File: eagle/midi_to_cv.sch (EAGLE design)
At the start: 45 parts, among them IC2 4504N, IC3 4099N, U1 ATMEGA328P_PDIP

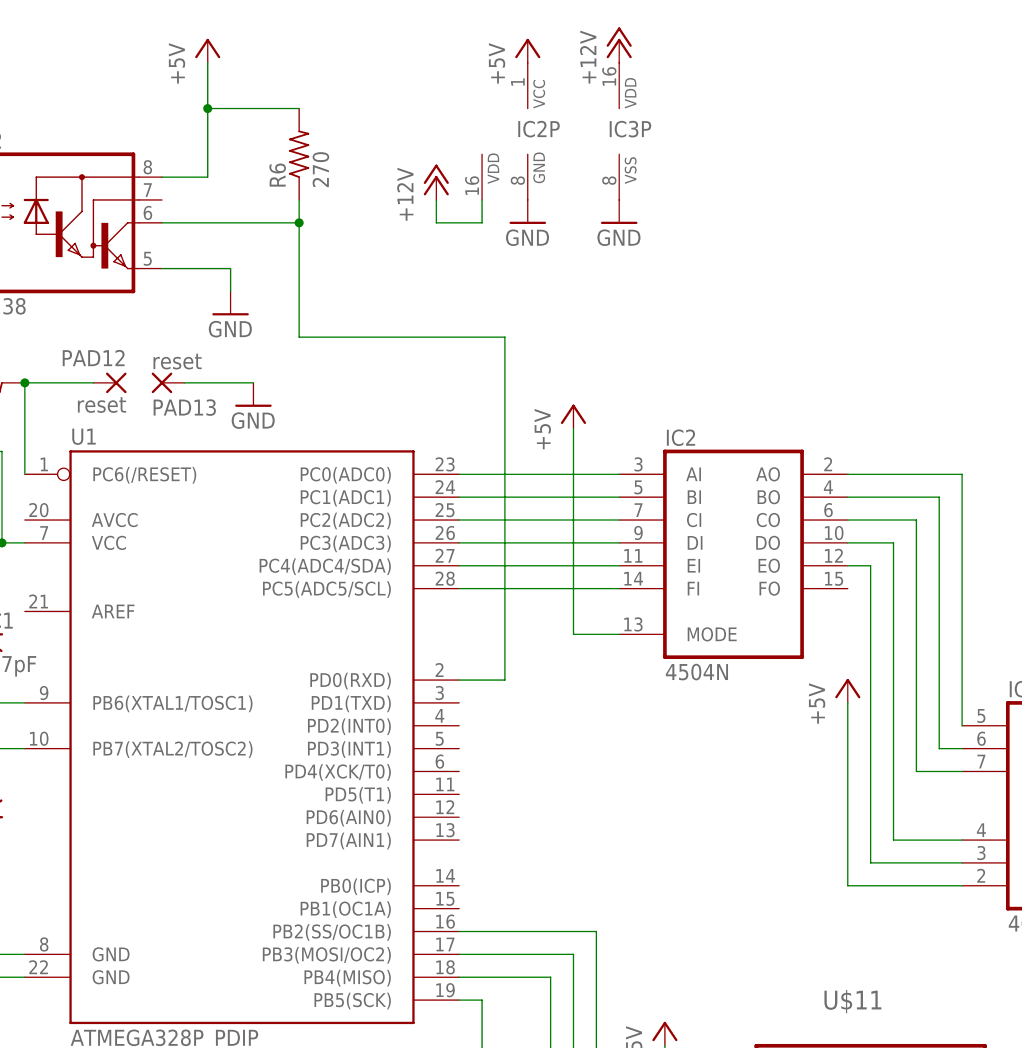
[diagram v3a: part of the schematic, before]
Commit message: connected midi to serial in
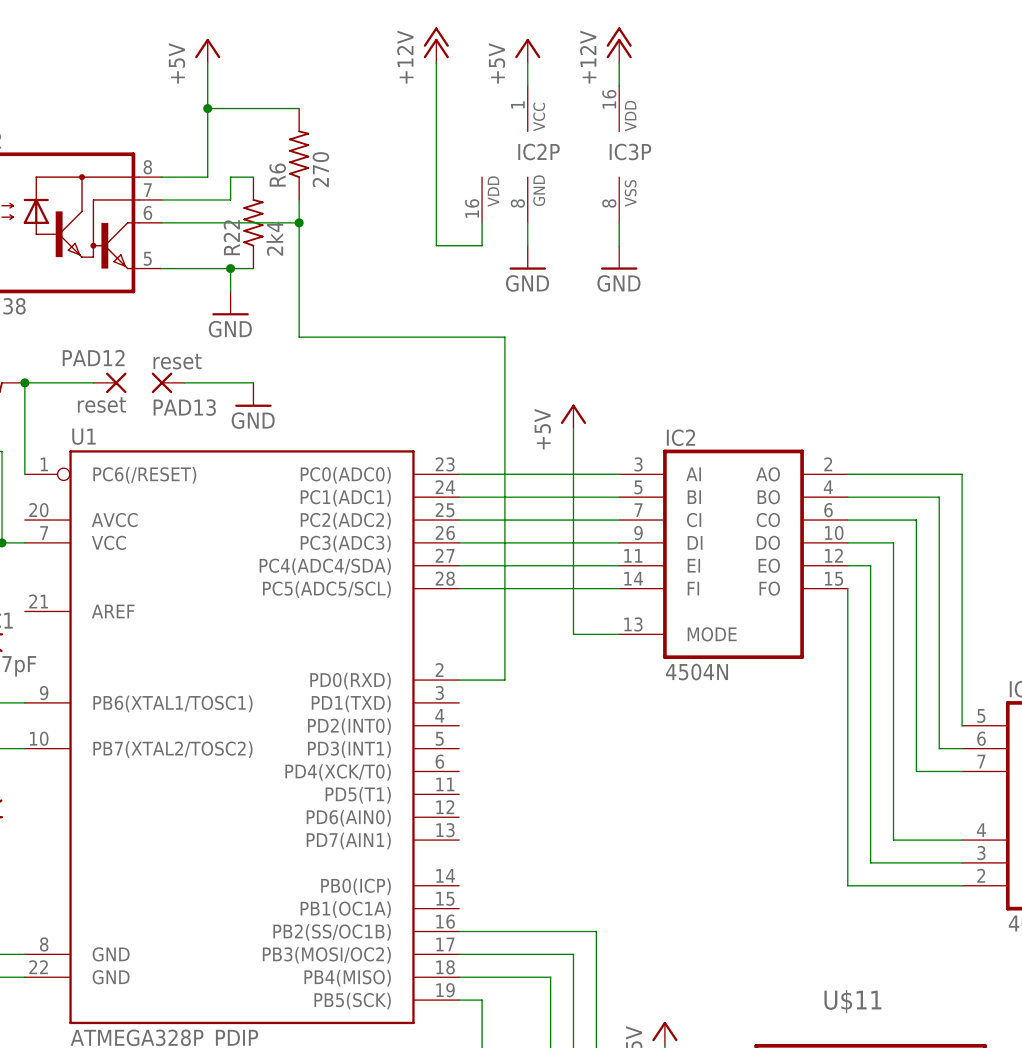
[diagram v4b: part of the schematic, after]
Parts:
- added R22: 2k4, rcl:R-US_0207/10
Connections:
- removed net N$30: U1.PD0(RXD)
- new net N$60: OK2.VB, R22.2
- new net N$61: IC2A.FO, IC3A.CLR
- net +5V: no longer IC3A.CLR
- net GND: now also R22.1
- net N$20: now also U1.PD0(RXD)
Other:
- moved on the sheet: IC2P, IC3P
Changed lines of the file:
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@@
 <part name="MIDI_IN" library="con-molex" deviceset="22-23-2021" device=""/>
 <part name="GND4" library="supply1" deviceset="GND" device=""/>
-<part name="P+2" library="supply1" deviceset="+5V" device=""/>
 <part name="U$11" library="Texas Instruments_By_element14_Batch_1" deviceset="TLV5628C/I" device=""/>
 <part name="P+5" library="supply1" deviceset="+5V" device=""/>
@@
 <part name="JP2" library="pinhead" deviceset="PINHD-1X8" device=""/>
 <part name="JP3" library="pinhead" deviceset="PINHD-1X8" device=""/>
+<part name="R22" library="rcl" deviceset="R-US_" device="0207/10" value="2k4"/>
 </parts>
 <sheets>
@@
 <instance part="R15" gate="G$1" x="-20.32" y="45.72" rot="R90"/>
 <instance part="IC2" gate="A" x="73.66" y="66.04"/>
-<instance part="IC2" gate="P" x="50.8" y="111.76"/>
+<instance part="IC2" gate="P" x="50.8" y="109.22"/>
 <instance part="IC3" gate="A" x="111.76" y="38.1"/>
-<instance part="IC3" gate="P" x="60.96" y="111.76"/>
+<instance part="IC3" gate="P" x="60.96" y="109.22"/>
 <instance part="P+4" gate="1" x="50.8" y="121.92"/>
-<instance part="P+8" gate="1" x="40.64" y="106.68"/>
-<instance part="GND3" gate="1" x="50.8" y="101.6"/>
-<instance part="GND16" gate="1" x="60.96" y="101.6"/>
+<instance part="P+8" gate="1" x="40.64" y="121.92"/>
+<instance part="GND3" gate="1" x="50.8" y="96.52"/>
+<instance part="GND16" gate="1" x="60.96" y="96.52"/>
 <instance part="P+15" gate="1" x="60.96" y="121.92"/>
 <instance part="P+16" gate="1" x="55.88" y="81.28"/>
@@
 <instance part="MIDI_IN" gate="-2" x="-38.1" y="96.52" rot="MR0"/>
 <instance part="GND4" gate="1" x="17.78" y="91.44"/>
-<instance part="P+2" gate="1" x="86.36" y="50.8"/>
 <instance part="U$11" gate="G$1" x="88.9" y="-12.7"/>
 <instance part="P+5" gate="1" x="66.04" y="12.7"/>
@@
 <instance part="JP2" gate="A" x="182.88" y="33.02" rot="R180"/>
 <instance part="JP3" gate="A" x="182.88" y="7.62" rot="R180"/>
+<instance part="R22" gate="G$1" x="20.32" y="101.6" rot="R90"/>
 </instances>
 <busses>
@@
 <pinref part="IC2" gate="P" pin="VCC"/>
 <pinref part="P+4" gate="1" pin="+5V"/>
+<wire x1="50.8" y1="116.84" x2="50.8" y2="119.38" width="0.1524" layer="91"/>
 </segment>
 <segment>
@@
 <wire x1="15.24" y1="119.38" x2="15.24" y2="114.3" width="0.1524" layer="91"/>
 <junction x="15.24" y="114.3"/>
-</segment>
-<segment>
-<pinref part="P+2" gate="1" pin="+5V"/>
-<wire x1="86.36" y1="48.26" x2="86.36" y2="27.94" width="0.1524" layer="91"/>
-<pinref part="IC3" gate="A" pin="CLR"/>
-<wire x1="86.36" y1="27.94" x2="99.06" y2="27.94" width="0.1524" layer="91"/>
 </segment>
 <segment>
@@
 <pinref part="IC2" gate="P" pin="GND"/>
 <pinref part="GND3" gate="1" pin="GND"/>
+<wire x1="50.8" y1="99.06" x2="50.8" y2="101.6" width="0.1524" layer="91"/>
 </segment>
 <segment>
 <pinref part="IC3" gate="P" pin="VSS"/>
 <pinref part="GND16" gate="1" pin="GND"/>
+<wire x1="60.96" y1="99.06" x2="60.96" y2="101.6" width="0.1524" layer="91"/>
 </segment>
 <segment>
@@
 <wire x1="10.16" y1="96.52" x2="17.78" y2="96.52" width="0.1524" layer="91"/>
 <pinref part="GND4" gate="1" pin="GND"/>
+<pinref part="R22" gate="G$1" pin="1"/>
+<wire x1="20.32" y1="96.52" x2="17.78" y2="96.52" width="0.1524" layer="91"/>
+<junction x="17.78" y="96.52"/>
 </segment>
 <segment>
@@
 <segment>
 <pinref part="P+8" gate="1" pin="+12V"/>
-<wire x1="40.64" y1="104.14" x2="40.64" y2="101.6" width="0.1524" layer="91"/>
+<wire x1="40.64" y1="119.38" x2="40.64" y2="99.06" width="0.1524" layer="91"/>
 <pinref part="IC2" gate="P" pin="VDD"/>
-<wire x1="40.64" y1="101.6" x2="45.72" y2="101.6" width="0.1524" layer="91"/>
-<wire x1="45.72" y1="101.6" x2="45.72" y2="104.14" width="0.1524" layer="91"/>
+<wire x1="40.64" y1="99.06" x2="45.72" y2="99.06" width="0.1524" layer="91"/>
+<wire x1="45.72" y1="99.06" x2="45.72" y2="101.6" width="0.1524" layer="91"/>
 </segment>
 <segment>
 <pinref part="IC3" gate="P" pin="VDD"/>
 <pinref part="P+15" gate="1" pin="+12V"/>
+<wire x1="60.96" y1="116.84" x2="60.96" y2="119.38" width="0.1524" layer="91"/>
 </segment>
 </net>
@@
 <pinref part="U$11" gate="G$1" pin="DATA"/>
 <wire x1="53.34" y1="-17.78" x2="71.12" y2="-17.78" width="0.1524" layer="91"/>
-</segment>
-</net>
-<net name="N$30" class="0">
-<segment>
-<pinref part="U1" gate="G$1" pin="PD0(RXD)"/>
-<wire x1="43.18" y1="50.8" x2="48.26" y2="50.8" width="0.1524" layer="91"/>
-<wire x1="48.26" y1="50.8" x2="48.26" y2="88.9" width="0.1524" layer="91"/>
-<wire x1="25.4" y1="88.9" x2="48.26" y2="88.9" width="0.1524" layer="91"/>
 </segment>
 </net>
@@
 <wire x1="25.4" y1="101.6" x2="25.4" y2="88.9" width="0.1524" layer="91"/>
 <junction x="25.4" y="101.6"/>
+<pinref part="U1" gate="G$1" pin="PD0(RXD)"/>
+<wire x1="43.18" y1="50.8" x2="48.26" y2="50.8" width="0.1524" layer="91"/>
+<wire x1="48.26" y1="50.8" x2="48.26" y2="88.9" width="0.1524" layer="91"/>
+<wire x1="25.4" y1="88.9" x2="48.26" y2="88.9" width="0.1524" layer="91"/>
 </segment>
 </net>
@@
 </segment>
 </net>
+<net name="N$60" class="0">
+<segment>
+<pinref part="OK2" gate="G$1" pin="VB"/>
+<wire x1="10.16" y1="104.14" x2="17.78" y2="104.14" width="0.1524" layer="91"/>
+<wire x1="17.78" y1="104.14" x2="17.78" y2="106.68" width="0.1524" layer="91"/>
+<pinref part="R22" gate="G$1" pin="2"/>
+<wire x1="17.78" y1="106.68" x2="20.32" y2="106.68" width="0.1524" layer="91"/>
+</segment>
+</net>
+<net name="N$61" class="0">
+<segment>
+<wire x1="86.36" y1="60.96" x2="86.36" y2="27.94" width="0.1524" layer="91"/>
+<pinref part="IC3" gate="A" pin="CLR"/>
+<wire x1="86.36" y1="27.94" x2="99.06" y2="27.94" width="0.1524" layer="91"/>
+<pinref part="IC2" gate="A" pin="FO"/>
+</segment>
+</net>

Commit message: ever closer to a route
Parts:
- C3: value .1uF -> 100n
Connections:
- removed net N$32 (its old number): IC2A.DI, U1.PC3(ADC3)
- removed net N$43: IC2A.FI, U1.PC5(ADC5/SCL)
- new net N$30: IC2A.AI, U1.PC2(ADC2)
- new net N$34: IC2A.DI, U1.PC5(ADC5/SCL)
- net N$23: now also IC2A.CI; no longer IC2A.AI
- net N$31: now also IC2A.FI, U1.PC3(ADC3); no longer IC2A.CI, U1.PC2(ADC2)
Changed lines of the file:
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@@
 <part name="C2" library="rcl" deviceset="C-US" device="025-040X050" value="27pF"/>
 <part name="R1" library="rcl" deviceset="R-US_" device="0207/10" value="10k"/>
-<part name="C3" library="rcl" deviceset="C-US" device="025-040X050" value=".1uF"/>
+<part name="C3" library="rcl" deviceset="C-US" device="025-040X050" value="100n"/>
 <part name="P+1" library="supply1" deviceset="+5V" device=""/>
 <part name="GND1" library="supply1" deviceset="GND" device=""/>
@@
 </segment>
 </net>
-<net name="N$23" class="0">
-<segment>
-<pinref part="U1" gate="G$1" pin="PC0(ADC0)"/>
-<pinref part="IC2" gate="A" pin="AI"/>
-<wire x1="43.18" y1="73.66" x2="60.96" y2="73.66" width="0.1524" layer="91"/>
-</segment>
-</net>
-<net name="N$25" class="0">
-<segment>
-<pinref part="U1" gate="G$1" pin="PC1(ADC1)"/>
-<pinref part="IC2" gate="A" pin="BI"/>
-<wire x1="43.18" y1="71.12" x2="60.96" y2="71.12" width="0.1524" layer="91"/>
-</segment>
-</net>
-<net name="N$31" class="0">
-<segment>
-<pinref part="U1" gate="G$1" pin="PC2(ADC2)"/>
-<pinref part="IC2" gate="A" pin="CI"/>
-<wire x1="43.18" y1="68.58" x2="60.96" y2="68.58" width="0.1524" layer="91"/>
-</segment>
-</net>
-<net name="N$32" class="0">
-<segment>
-<pinref part="IC2" gate="A" pin="DI"/>
-<pinref part="U1" gate="G$1" pin="PC3(ADC3)"/>
-<wire x1="60.96" y1="66.04" x2="43.18" y2="66.04" width="0.1524" layer="91"/>
-</segment>
-</net>
-<net name="N$34" class="0">
-<segment>
-<pinref part="U1" gate="G$1" pin="PC4(ADC4/SDA)"/>
-<pinref part="IC2" gate="A" pin="EI"/>
-<wire x1="43.18" y1="63.5" x2="60.96" y2="63.5" width="0.1524" layer="91"/>
-</segment>
-</net>
-<net name="N$43" class="0">
-<segment>
-<pinref part="IC2" gate="A" pin="FI"/>
-<pinref part="U1" gate="G$1" pin="PC5(ADC5/SCL)"/>
-<wire x1="60.96" y1="60.96" x2="43.18" y2="60.96" width="0.1524" layer="91"/>
-</segment>
-</net>
 <net name="N$39" class="0">
 <segment>
@@
 </segment>
 </net>
+<net name="N$23" class="0">
+<segment>
+<pinref part="U1" gate="G$1" pin="PC0(ADC0)"/>
+<pinref part="IC2" gate="A" pin="CI"/>
+<wire x1="43.18" y1="73.66" x2="60.96" y2="68.58" width="0.1524" layer="91"/>
+</segment>
+</net>
+<net name="N$25" class="0">
+<segment>
+<pinref part="IC2" gate="A" pin="BI"/>
+<pinref part="U1" gate="G$1" pin="PC1(ADC1)"/>
+<wire x1="60.96" y1="71.12" x2="43.18" y2="71.12" width="0.1524" layer="91"/>
+</segment>
+</net>
+<net name="N$30" class="0">
+<segment>
+<pinref part="U1" gate="G$1" pin="PC2(ADC2)"/>
+<pinref part="IC2" gate="A" pin="AI"/>
+<wire x1="43.18" y1="68.58" x2="60.96" y2="73.66" width="0.1524" layer="91"/>
+</segment>
+</net>
+<net name="N$31" class="0">
+<segment>
+<pinref part="U1" gate="G$1" pin="PC3(ADC3)"/>
+<pinref part="IC2" gate="A" pin="FI"/>
+<wire x1="43.18" y1="66.04" x2="60.96" y2="60.96" width="0.1524" layer="91"/>
+</segment>
+</net>
+<net name="N$32" class="0">
+<segment>
+<pinref part="IC2" gate="A" pin="EI"/>
+<pinref part="U1" gate="G$1" pin="PC4(ADC4/SDA)"/>
+<wire x1="60.96" y1="63.5" x2="43.18" y2="63.5" width="0.1524" layer="91"/>
+</segment>
+</net>
+<net name="N$34" class="0">
+<segment>
+<pinref part="U1" gate="G$1" pin="PC5(ADC5/SCL)"/>
+<pinref part="IC2" gate="A" pin="DI"/>
+<wire x1="43.18" y1="60.96" x2="60.96" y2="66.04" width="0.1524" layer="91"/>
+</segment>
+</net>
